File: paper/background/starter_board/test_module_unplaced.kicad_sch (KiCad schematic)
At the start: 15 parts, among them J1 Barrel_Jack_12V, J2 RS232_2CH_Module, M1 ERM_Motor, M2 Stepper_4wire, M3 Servo_3pin, U1 D24V22F5_Buck, U2 Pi_Pico_W, U3 DRV2605L_Breakout, U4 DRV8871_Breakout, U5 Tic_T500

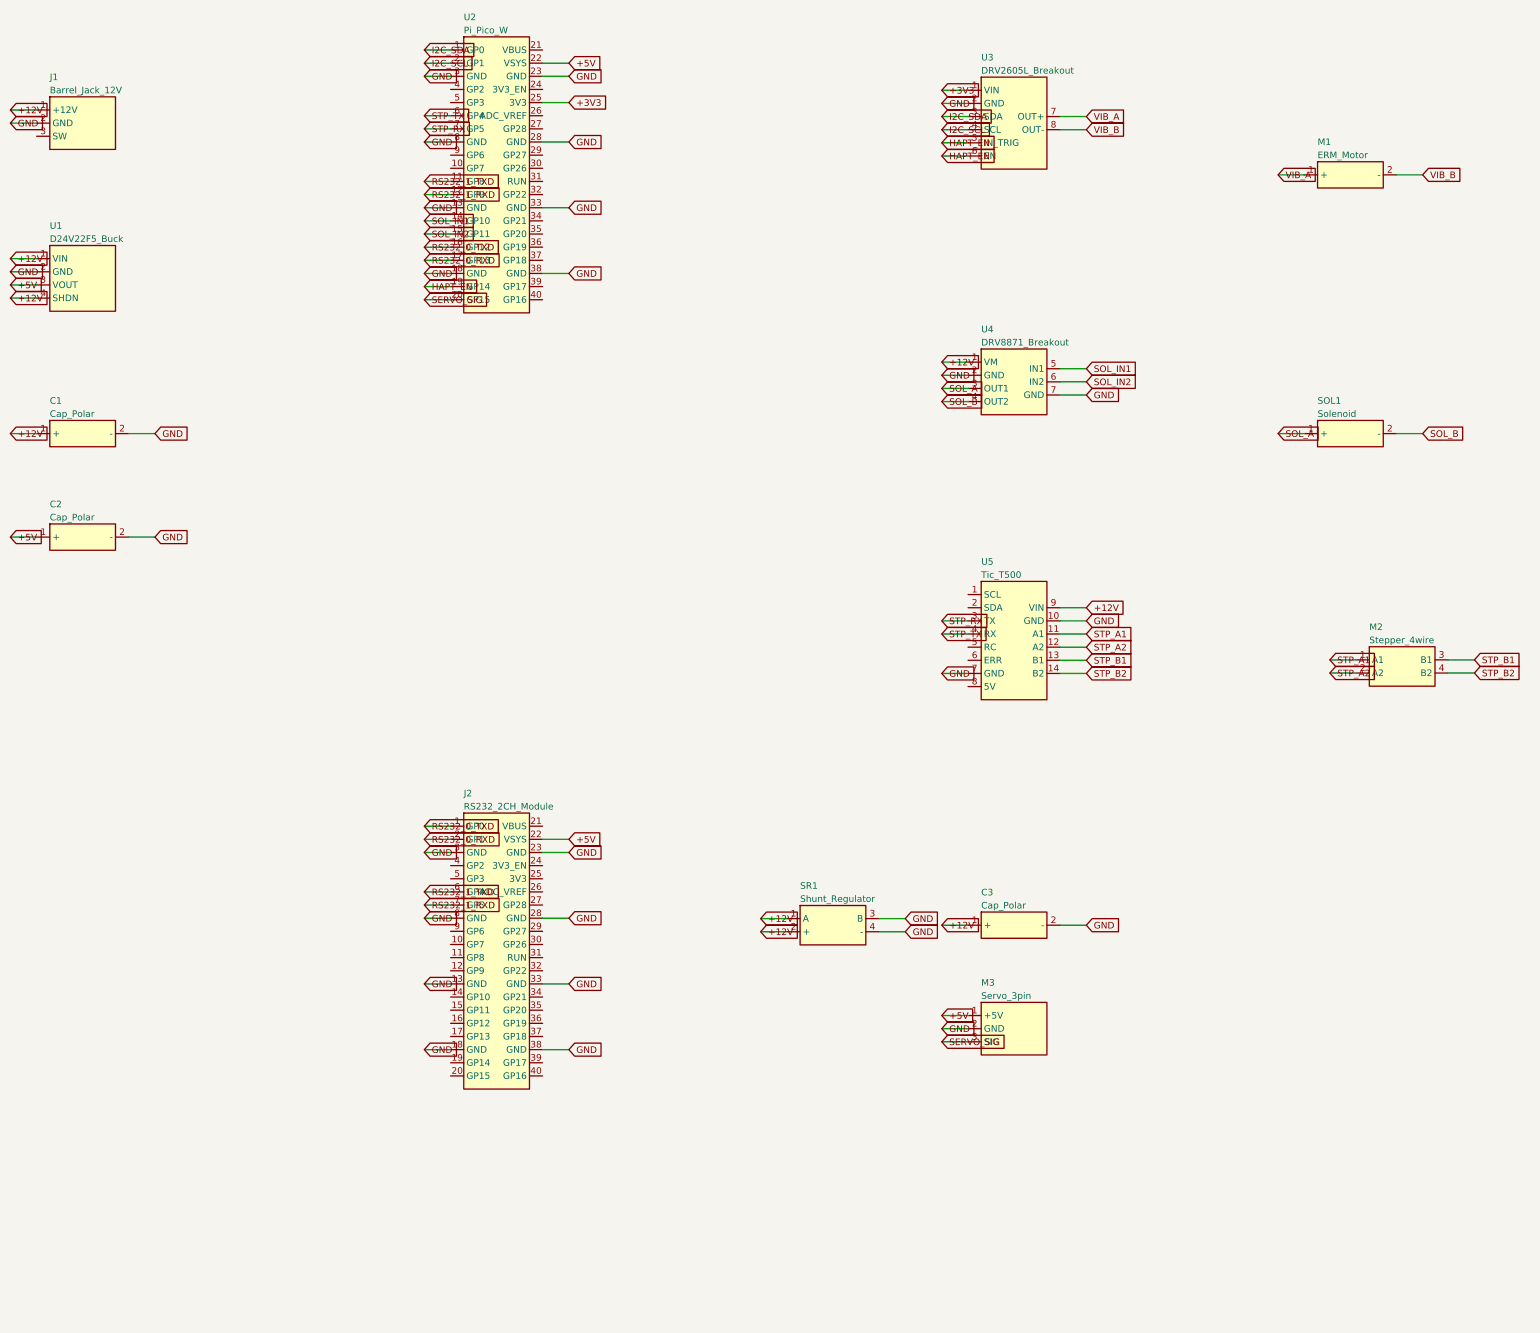
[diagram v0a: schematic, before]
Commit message: Align starter-board KiCad trios with PR #100 scale integration (U6 RS-232 on +3V3, SCALE_TX/RX)
Regenerates both upload trios from PR #100's rev B netlist: the Waveshare
Pico-2CH-RS232 becomes U6 reached via its channel-0 4-pin TTL header
(VCC on +3V3 so the TTL swing stays inside the RP2040 abs max), wired
straight across on UART0 (GP12->TXD = SCALE_TX, GP13<-RXD = SCALE_RX);
the 40-pad J2 receptacle model and the spare GP8/GP9 channel nets are
dropped. Board is now 15 footprints / 101 pads / 75 net-assigned /
22 nets. Verified: kicad-cli netlist (75 pins, 22 nets, zero
unconnected), pcbnew DRC (0 courtyard/clearance errors, both trios),
15<->15 footprint<->symbol UUID bijection, byte-for-byte reproducible,
netlist cross-checked ref-by-ref against PR #100's PLACEMENTS
(identical 22-net set), and PR #100's ngspice RS-232 interface
analysis re-run (9/9 PASS).

Co-authored-by: Luke Blaine Winters <288785662+lbwinters@users.noreply.github.com>
Co-Authored-By: Claude Fable 5 <noreply@anthropic.com>
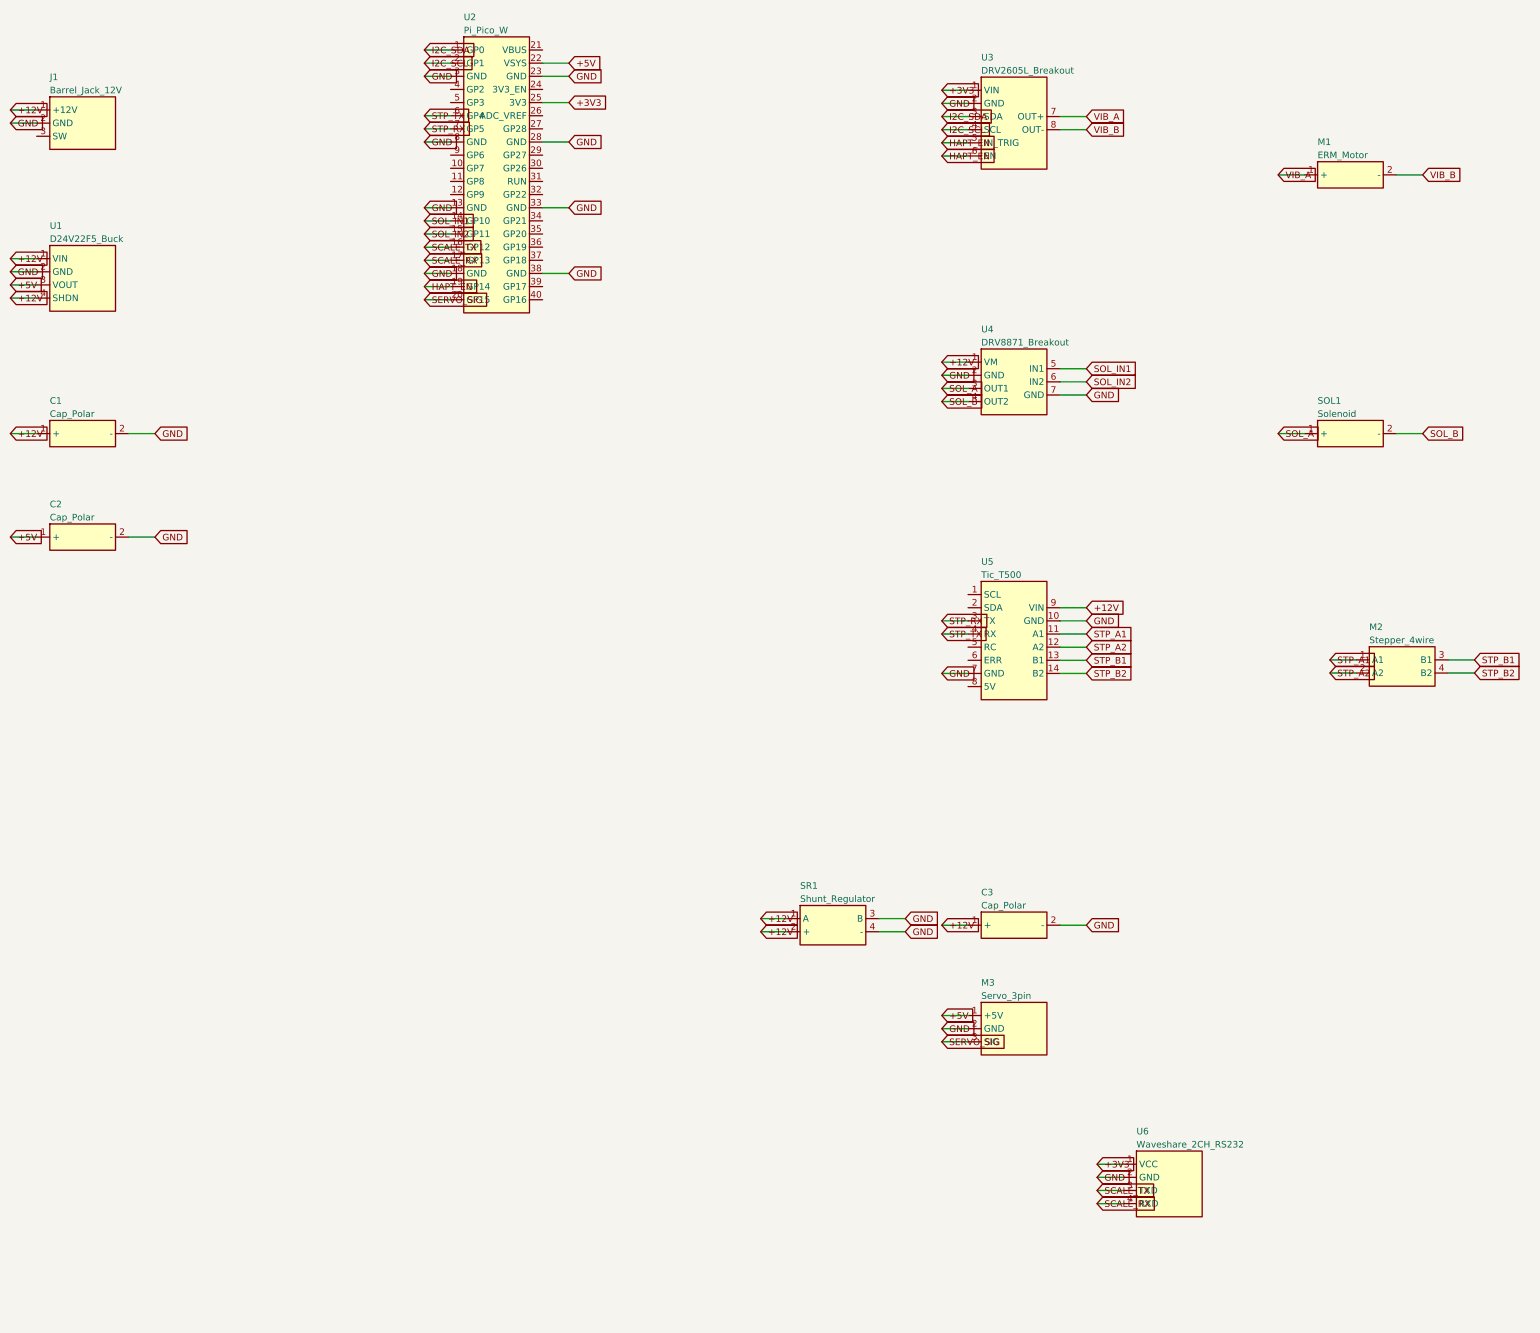
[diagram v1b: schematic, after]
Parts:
- removed J2: RS232_2CH_Module, powder_doser_parts:RS232_2CH_Module, symbol powder_doser_parts:RS232_2CH_Module
- added U6: Waveshare_2CH_RS232, powder_doser_parts:Waveshare_2CH_RS232, symbol powder_doser_parts:Waveshare_2CH_RS232
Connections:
- net +3V3: now also U6.1 (VCC)
- net GND: now also U6.2 (GND)
- net RS232_0_RXD renamed SCALE_RX
- net SCALE_RX: now also U6.4 (RXD)
- net RS232_0_TXD renamed SCALE_TX
- net SCALE_TX: now also U6.3 (TXD)
- net RS232_1_RXD: no longer names the net of U2.12 (GP9)
- net RS232_1_TXD: no longer names the net of U2.11 (GP8)
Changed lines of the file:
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@@
-    (effects (font (size 1.27 1.27)) (justify left))
-  )
-  (wire (pts (xy 101.11 51.27) (xy 96.03 51.27))
-    (stroke (width 0) (type default))
-  )
-  (global_label "RS232_1_TXD" (shape input) (at 96.03 51.27 180) (fields_autoplaced)
-    (effects (font (size 1.27 1.27)) (justify left))
-  )
-  (wire (pts (xy 101.11 53.81) (xy 96.03 53.81))
-    (stroke (width 0) (type default))
-  )
-  (global_label "RS232_1_RXD" (shape input) (at 96.03 53.81 180) (fields_autoplaced)
     (effects (font (size 1.27 1.27)) (justify left))
   )
@@
     (stroke (width 0) (type default))
   )
-  (global_label "RS232_0_TXD" (shape input) (at 96.03 63.97 180) (fields_autoplaced)
+  (global_label "SCALE_TX" (shape input) (at 96.03 63.97 180) (fields_autoplaced)
     (effects (font (size 1.27 1.27)) (justify left))
   )
@@
     (stroke (width 0) (type default))
   )
-  (global_label "RS232_0_RXD" (shape input) (at 96.03 66.51 180) (fields_autoplaced)
+  (global_label "SCALE_RX" (shape input) (at 96.03 66.51 180) (fields_autoplaced)
     (effects (font (size 1.27 1.27)) (justify left))
   )
@@
     (effects (font (size 1.27 1.27)) (justify left))
   )
-  (symbol (lib_id "powder_doser_parts:RS232_2CH_Module") (at 110 200 0) (unit 1)
-    (in_bom yes) (on_board yes) (dnp no)
-    (property "Reference" "J2" (id 0) (at 103.65 169.52 0)
-      (effects (font (size 1.27 1.27)) (justify left)))
-    (property "Value" "RS232_2CH_Module" (id 1) (at 103.65 172.06 0)
-      (effects (font (size 1.27 1.27)) (justify left)))
-    (property "Footprint" "powder_doser_parts:RS232_2CH_Module" (id 2) (at 110 200 0)
-      (effects (font (size 1.27 1.27)) hide))
-    (property "Datasheet" "" (id 3) (at 110 200 0)
-      (effects (font (size 1.27 1.27)) hide))
-    (instances
-      (project "test_module_unplaced"
-        (path "/00000000-0000-0000-0003-000000000001" (reference "J2") (unit 1))
-      )
-    )
-  )
-  (wire (pts (xy 101.11 175.87) (xy 96.03 175.87))
-    (stroke (width 0) (type default))
-  )
-  (global_label "RS232_0_TXD" (shape input) (at 96.03 175.87 180) (fields_autoplaced)
-    (effects (font (size 1.27 1.27)) (justify left))
-  )
-  (wire (pts (xy 101.11 178.41) (xy 96.03 178.41))
-    (stroke (width 0) (type default))
-  )
-  (global_label "RS232_0_RXD" (shape input) (at 96.03 178.41 180) (fields_autoplaced)
-    (effects (font (size 1.27 1.27)) (justify left))
-  )
-  (wire (pts (xy 101.11 180.95) (xy 96.03 180.95))
-    (stroke (width 0) (type default))
-  )
-  (global_label "GND" (shape input) (at 96.03 180.95 180) (fields_autoplaced)
-    (effects (font (size 1.27 1.27)) (justify left))
-  )
-  (wire (pts (xy 101.11 188.57) (xy 96.03 188.57))
-    (stroke (width 0) (type default))
-  )
-  (global_label "RS232_1_TXD" (shape input) (at 96.03 188.57 180) (fields_autoplaced)
-    (effects (font (size 1.27 1.27)) (justify left))
-  )
-  (wire (pts (xy 101.11 191.11) (xy 96.03 191.11))
-    (stroke (width 0) (type default))
-  )
-  (global_label "RS232_1_RXD" (shape input) (at 96.03 191.11 180) (fields_autoplaced)
-    (effects (font (size 1.27 1.27)) (justify left))
-  )
-  (wire (pts (xy 101.11 193.65) (xy 96.03 193.65))
-    (stroke (width 0) (type default))
-  )
-  (global_label "GND" (shape input) (at 96.03 193.65 180) (fields_autoplaced)
-    (effects (font (size 1.27 1.27)) (justify left))
-  )
-  (wire (pts (xy 101.11 206.35) (xy 96.03 206.35))
-    (stroke (width 0) (type default))
-  )
-  (global_label "GND" (shape input) (at 96.03 206.35 180) (fields_autoplaced)
-    (effects (font (size 1.27 1.27)) (justify left))
-  )
-  (wire (pts (xy 101.11 219.05) (xy 96.03 219.05))
-    (stroke (width 0) (type default))
-  )
-  (global_label "GND" (shape input) (at 96.03 219.05 180) (fields_autoplaced)
-    (effects (font (size 1.27 1.27)) (justify left))
-  )
-  (wire (pts (xy 118.89 178.41) (xy 123.97 178.41))
-    (stroke (width 0) (type default))
-  )
-  (global_label "+5V" (shape input) (at 123.97 178.41 0) (fields_autoplaced)
-    (effects (font (size 1.27 1.27)) (justify left))
-  )
-  (wire (pts (xy 118.89 180.95) (xy 123.97 180.95))
-    (stroke (width 0) (type default))
-  )
-  (global_label "GND" (shape input) (at 123.97 180.95 0) (fields_autoplaced)
-    (effects (font (size 1.27 1.27)) (justify left))
-  )
-  (wire (pts (xy 118.89 193.65) (xy 123.97 193.65))
-    (stroke (width 0) (type default))
-  )
-  (global_label "GND" (shape input) (at 123.97 193.65 0) (fields_autoplaced)
-    (effects (font (size 1.27 1.27)) (justify left))
-  )
-  (wire (pts (xy 118.89 206.35) (xy 123.97 206.35))
-    (stroke (width 0) (type default))
-  )
-  (global_label "GND" (shape input) (at 123.97 206.35 0) (fields_autoplaced)
-    (effects (font (size 1.27 1.27)) (justify left))
-  )
-  (wire (pts (xy 118.89 219.05) (xy 123.97 219.05))
-    (stroke (width 0) (type default))
-  )
-  (global_label "GND" (shape input) (at 123.97 219.05 0) (fields_autoplaced)
-    (effects (font (size 1.27 1.27)) (justify left))
-  )
+  (symbol (lib_id "powder_doser_parts:Waveshare_2CH_RS232") (at 240 245 0) (unit 1)
+    (in_bom yes) (on_board yes) (dnp no)
+    (property "Reference" "U6" (id 0) (at 233.65 234.84 0)
+      (effects (font (size 1.27 1.27)) (justify left)))
+    (property "Value" "Waveshare_2CH_RS232" (id 1) (at 233.65 237.38 0)
+      (effects (font (size 1.27 1.27)) (justify left)))
+    (property "Footprint" "powder_doser_parts:Waveshare_2CH_RS232" (id 2) (at 240 245 0)
+      (effects (font (size 1.27 1.27)) hide))
+    (property "Datasheet" "" (id 3) (at 240 245 0)
+      (effects (font (size 1.27 1.27)) hide))
+    (instances
+      (project "test_module_unplaced"
+        (path "/00000000-0000-0000-0003-000000000001" (reference "U6") (unit 1))
+      )
+    )
+  )
+  (wire (pts (xy 231.11 241.19) (xy 226.03 241.19))
+    (stroke (width 0) (type default))
+  )
+  (global_label "+3V3" (shape input) (at 226.03 241.19 180) (fields_autoplaced)
+    (effects (font (size 1.27 1.27)) (justify left))
+  )
+  (wire (pts (xy 231.11 243.73) (xy 226.03 243.73))
+    (stroke (width 0) (type default))
+  )
+  (global_label "GND" (shape input) (at 226.03 243.73 180) (fields_autoplaced)
+    (effects (font (size 1.27 1.27)) (justify left))
+  )
+  (wire (pts (xy 231.11 246.27) (xy 226.03 246.27))
+    (stroke (width 0) (type default))
+  )
+  (global_label "SCALE_TX" (shape input) (at 226.03 246.27 180) (fields_autoplaced)
+    (effects (font (size 1.27 1.27)) (justify left))
+  )
+  (wire (pts (xy 231.11 248.81) (xy 226.03 248.81))
+    (stroke (width 0) (type default))
+  )
+  (global_label "SCALE_RX" (shape input) (at 226.03 248.81 180) (fields_autoplaced)
+    (effects (font (size 1.27 1.27)) (justify left))
+  )
